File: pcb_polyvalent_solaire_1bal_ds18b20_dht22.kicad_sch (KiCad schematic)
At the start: 19 parts, among them J1 Conn_01x12, J10 Conn_01x08, J11 Conn_01x05, J12 Conn_01x02, J13 Conn_01x02, J14 Conn_01x02, J15 Conn_01x03, J2 Conn_01x12, J3 Conn_01x15, J4 Conn_01x15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

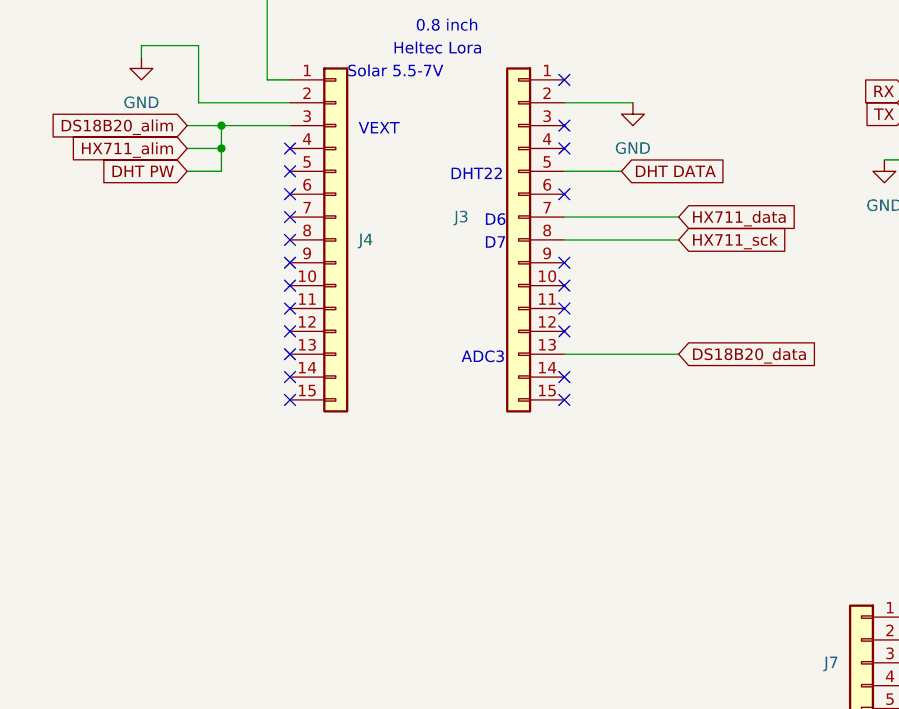
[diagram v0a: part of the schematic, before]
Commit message: schémat modifié data dht22 passe de la pin5 à la pin 6 qui est le gpio5
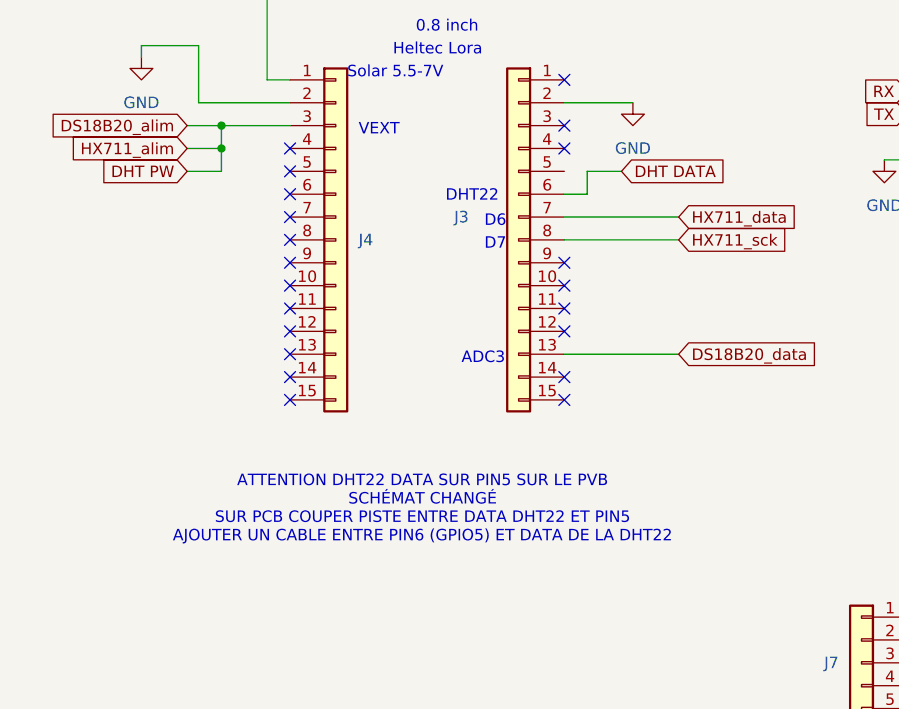
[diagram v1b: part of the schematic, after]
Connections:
- net DHT DATA: now also J3.6 (Pin_6); no longer J3.5 (Pin_5)
- no-connect marks 34 -> 33
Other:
- note added: "ATTENTION DHT22 DATA SUR PIN5 SUR LE PVB SCHÉMAT CHANGÉ SUR PCB COUPER PISTE ENTRE DATA DHT22 ET PIN5 AJOUTER UN CABLE ENTRE PIN6 (GPIO5) ET DATA DE LA DHT22"
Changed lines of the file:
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@@
-	)
-	(no_connect
-		(at 78.74 86.36)
 	)
 	(no_connect
@@
 	(wire
 		(pts
+			(xy 81.28 83.82) (xy 81.28 86.36)
+		)
+		(stroke
+			(width 0)
+			(type default)
+		)
+	)
+	(wire
+		(pts
 			(xy 116.84 143.51) (xy 120.65 143.51)
 		)
@@
 	(wire
 		(pts
+			(xy 81.28 86.36) (xy 78.74 86.36)
+		)
+		(stroke
+			(width 0)
+			(type default)
+		)
+	)
+	(wire
+		(pts
 			(xy 115.57 29.21) (xy 100.33 29.21)
 		)
@@
 	(wire
 		(pts
+			(xy 85.09 83.82) (xy 81.28 83.82)
+		)
+		(stroke
+			(width 0)
+			(type default)
+		)
+	)
+	(wire
+		(pts
 			(xy 116.84 138.43) (xy 120.65 138.43)
 		)
@@
 	(wire
 		(pts
-			(xy 78.74 83.82) (xy 85.09 83.82)
-		)
-		(stroke
-			(width 0)
-			(type default)
-		)
-	)
-	(wire
-		(pts
 			(xy 78.74 88.9) (xy 91.44 88.9)
 		)
@@
 		)
 	)
+	(text "ATTENTION DHT22 DATA SUR PIN5 SUR LE PVB\nSCHÉMAT CHANGÉ\nSUR PCB COUPER PISTE ENTRE DATA DHT22 ET PIN5\nAJOUTER UN CABLE ENTRE PIN6 (GPIO5) ET DATA DE LA DHT22"
+		(exclude_from_sim no)
+		(at 62.992 121.412 0)
+		(effects
+			(font
+				(size 1.27 1.27)
+			)
+		)
+	)
 	(text "Solar charger\n4.4V à 6V"
 		(exclude_from_sim no)
@@
 	(text "DHT22"
 		(exclude_from_sim no)
-		(at 66.04 85.09 0)
-		(effects
-			(font
+		(at 65.532 87.376 0)
+		(effects
+			(font
